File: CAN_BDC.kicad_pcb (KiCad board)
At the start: 2 copper layers, 25 x 31.8 mm, 28 parts, among them P1 CONN_01X02, P2 CONN_01X05, P3 CONN_01X02, P4 CONN_01X04, P5 CONN_01X04, P6 CONN_01X02, P7 CONN_01X04, P8 CONN_01X04, P9 CONN_01X02, U1 PSD2CAN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

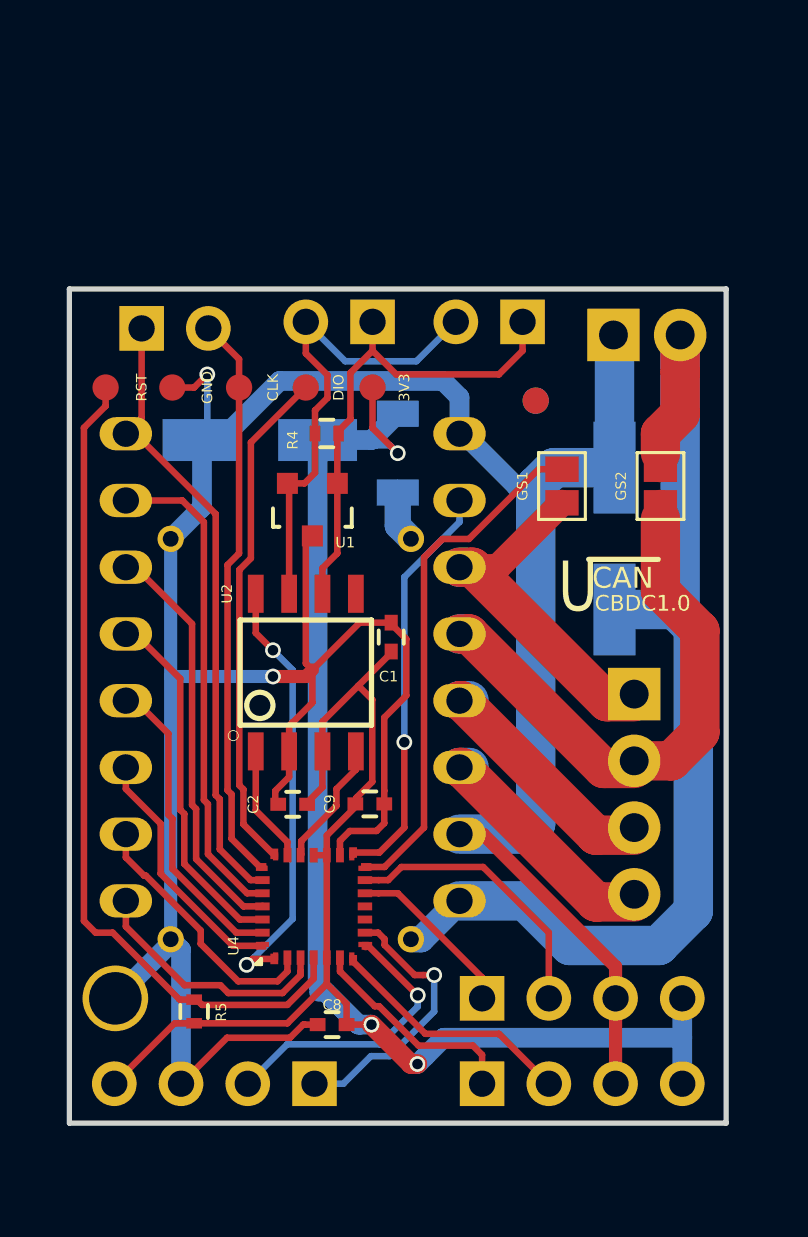
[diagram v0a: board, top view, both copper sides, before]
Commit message: Connector reposition
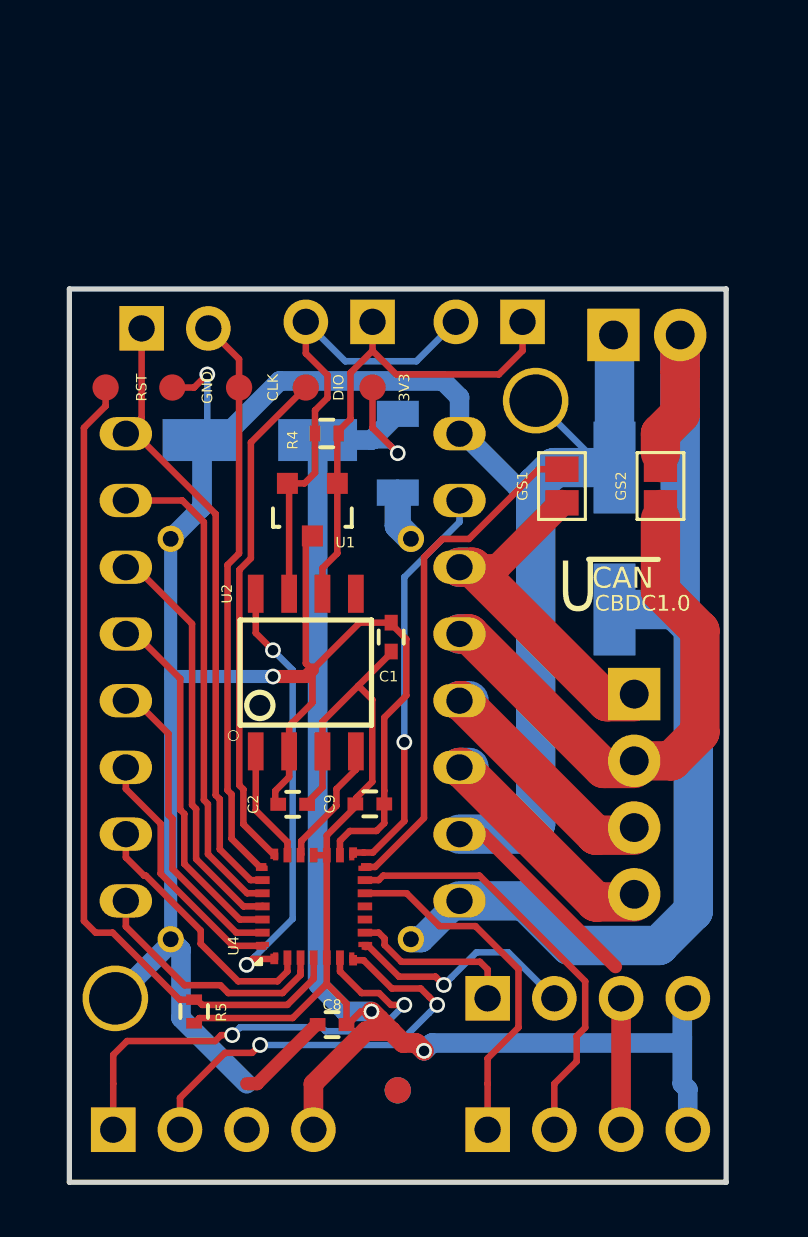
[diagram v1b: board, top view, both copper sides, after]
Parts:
- added mh2: fiducial, usb_ccb_custom:1pin, F.Cu at (156.4, 84.0)
- U3: value POLOLU_DRV8825 -> POLOLU_DRV8825/DRV8801
- moved f1 26.8 mm to (151.2, 110.3)
- moved f2 26.8 mm to (151.2, 110.3)
- moved P8 14.1 mm to (140.4, 111.8)
- moved P4 7.35 mm to (154.6, 106.8), turned to 270 degrees
- moved P5 5.00 mm to (154.6, 111.8)
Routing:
- net GPIO1: track 8.68 -> 18.3 mm, vias 0 -> 2
- net GPIO3: track 6.58 -> 13.6 mm
- net GPIO2: track 9.43 -> 16.4 mm, vias 0 -> 2
- net GPIO4: track 10.7 -> 16.3 mm
- net /USART_RX: track 10.5 -> 6.49 mm, vias 1 -> 0
- net GND: track 124.2 -> 126.7 mm
- net /USART_TX: track 10.9 -> 9.06 mm
- net +3V3: track 81.7 -> 82.7 mm
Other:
- board size 25 x 31.8 mm -> 25 x 34 mm

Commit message: CAN layout update
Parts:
- moved P3 1.50 mm to (141.4, 79.8)
- moved P1 1.25 mm to (150.2, 79.8)
- moved P9 1.25 mm to (155.9, 79.8)
- moved C7 0.15 mm to (146.1, 85.5)
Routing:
- net Net-(P1-Pad2): track 18.7 -> 22.2 mm
- net Net-(P1-Pad1): track 18.7 -> 20.9 mm
- net SW_CLK: track 21.7 -> 23.7 mm
- net DRV_DIR: track 24.7 -> 25.9 mm
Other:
- board size 25 x 34 mm -> 25 x 35.5 mm
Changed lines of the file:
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@@
   (general
     (links 85)
-    (no_connects 6)
-    (area 138.599999 79.699999 163.800001 113.900001)
+    (no_connects 2)
+    (area 138.599999 78.699999 163.800001 113.900001)
     (thickness 1.6)
     (drawings 13)
-    (tracks 391)
+    (tracks 403)
     (zones 0)
     (modules 29)
@@
   (page A4)
   (layers
-    (0 F.Cu signal hide)
-    (31 B.Cu signal hide)
+    (0 F.Cu signal)
+    (31 B.Cu signal)
     (32 B.Adhes user)
     (33 F.Adhes user)
@@
   )
   (module Capacitors_SMD:c_elec_5x5.8 (layer B.Cu)
-    (at 145.95 85.55 180)
+    (at 146.1 85.55 180)
     (descr "SMT capacitor, aluminium electrolytic, 5x5.8")
     (attr smd)
@@
   )
   (module Pin_Headers:Pin_Header_Straight_1x02_Pitch2.54mm (layer B.Cu)
-    (at 155.95 81.05 90)
+    (at 155.95 79.8 90)
     (descr "Through hole straight pin header, 1x02, 2.54mm pitch, single row")
     (tags "Through hole pin header THT 1x02 2.54mm single row")
@@
   )
   (module Pin_Headers:Pin_Header_Straight_1x02_Pitch2.54mm (layer B.Cu)
-    (at 150.24 81.05 90)
+    (at 150.24 79.8 90)
     (descr "Through hole straight pin header, 1x02, 2.54mm pitch, single row")
     (tags "Through hole pin header THT 1x02 2.54mm single row")
@@
   )
   (module Pin_Headers:Pin_Header_Straight_1x02_Pitch2.54mm (layer B.Cu)
-    (at 141.45 81.3 270)
+    (at 141.45 79.8 270)
     (descr "Through hole straight pin header, 1x02, 2.54mm pitch, single row")
     (tags "Through hole pin header THT 1x02 2.54mm single row")
@@
   )
   (gr_line (start 163.7 113.8) (end 138.7 113.8) (layer Edge.Cuts) (width 0.2))
-  (gr_line (start 163.7 79.8) (end 163.7 113.8) (layer Edge.Cuts) (width 0.2))
-  (gr_line (start 138.7 79.8) (end 163.7 79.8) (layer Edge.Cuts) (width 0.2))
-  (gr_line (start 138.7 113.8) (end 138.7 79.8) (layer Edge.Cuts) (width 0.2))
+  (gr_line (start 163.7 78.3) (end 163.7 113.8) (layer Edge.Cuts) (width 0.2))
+  (gr_line (start 138.7 78.3) (end 163.7 78.3) (layer Edge.Cuts) (width 0.2))
+  (gr_line (start 138.7 113.8) (end 138.7 78.3) (layer Edge.Cuts) (width 0.2))
   (gr_text GND (at 143.95 83.55 90) (layer F.SilkS)
     (effects (font (size 0.4 0.4) (thickness 0.1)))
@@
   )
   (gr_line (start 158.465484 90.090166) (end 161.111084 90.090166) (angle 90) (layer F.SilkS) (width 0.2))
+  (segment (start 147.7 81.05) (end 147.7 79.8) (width 0.25) (layer B.Cu) (net 1))
+  (segment (start 153.41 81.05) (end 153.41 79.8) (width 0.25) (layer B.Cu) (net 1))
+  (segment (start 147.7 82.252081) (end 147.7 81.3) (width 0.25) (layer F.Cu) (net 1))
+  (segment (start 147.7 81.3) (end 147.7 81.05) (width 0.25) (layer F.Cu) (net 1))
+  (segment (start 147.7 80.3) (end 147.7 81.3) (width 0.25) (layer F.Cu) (net 1))
   (segment (start 149.2 82.55) (end 151.91 82.55) (width 0.25) (layer B.Cu) (net 1))
   (segment (start 151.91 82.55) (end 153.41 81.05) (width 0.25) (layer B.Cu) (net 1))
@@
   (segment (start 148.525001 83.946001) (end 148.525001 83.077082) (width 0.25) (layer F.Cu) (net 1))
   (segment (start 148.525001 83.077082) (end 147.7 82.252081) (width 0.25) (layer F.Cu) (net 1))
-  (segment (start 147.7 82.252081) (end 147.7 81.05) (width 0.25) (layer F.Cu) (net 1))
   (segment (start 147 87.19924) (end 147.65005 87.19924) (width 0.25) (layer F.Cu) (net 1))
   (segment (start 147.65005 87.19924) (end 148.05 86.79929) (width 0.25) (layer F.Cu) (net 1))
@@
   (segment (start 148.5 101.35) (end 148 101.35) (width 0.25) (layer F.Cu) (net 3) (status 30))
   (segment (start 148.5 105.25) (end 148.5 101.593408) (width 0.25) (layer F.Cu) (net 3) (status 30))
+  (segment (start 143.99 80.8) (end 143.99 80.3) (width 0.25) (layer F.Cu) (net 4))
+  (segment (start 143.99 81.3) (end 143.99 80.8) (width 0.25) (layer F.Cu) (net 4))
+  (segment (start 143.99 80.8) (end 143.99 79.8) (width 0.25) (layer F.Cu) (net 4))
   (segment (start 145.16 83.55) (end 145.16 82.47) (width 0.25) (layer F.Cu) (net 4))
   (segment (start 145.16 82.47) (end 143.99 81.3) (width 0.25) (layer F.Cu) (net 4))
@@
   (segment (start 151.7 104.55) (end 152.09 104.55) (width 1) (layer B.Cu) (net 11) (status 30))
   (segment (start 152.09 104.55) (end 153.55 103.09) (width 1) (layer B.Cu) (net 11) (status 30))
+  (segment (start 155.95 81.05) (end 155.95 79.8) (width 0.25) (layer F.Cu) (net 12))
+  (segment (start 150.24 81.3) (end 150.24 81.05) (width 0.25) (layer F.Cu) (net 12))
+  (segment (start 150.24 81.3) (end 150.24 80.3) (width 0.25) (layer F.Cu) (net 12))
+  (segment (start 150.24 82.15) (end 150.24 81.3) (width 0.25) (layer F.Cu) (net 12))
   (segment (start 151.14 83.05) (end 155.05 83.05) (width 0.25) (layer F.Cu) (net 12))
   (segment (start 155.05 83.05) (end 155.95 82.15) (width 0.25) (layer F.Cu) (net 12))
@@
   (segment (start 149.4 84.75) (end 149.4 82.99) (width 0.25) (layer F.Cu) (net 12))
   (segment (start 148.95 85.2) (end 149.4 84.75) (width 0.25) (layer F.Cu) (net 12))
-  (segment (start 150.24 82.15) (end 150.24 81.05) (width 0.25) (layer F.Cu) (net 12))
   (segment (start 148.95 85.3) (end 148.95 85.2) (width 0.25) (layer F.Cu) (net 12))
   (segment (start 149.4 82.99) (end 150.24 82.15) (width 0.25) (layer F.Cu) (net 12))
@@
   (segment (start 143.975056 99.406753) (end 143.975056 101.310347) (width 0.25) (layer F.Cu) (net 15))
   (segment (start 145.464709 102.8) (end 146.05 102.8) (width 0.25) (layer F.Cu) (net 15) (status 20))
+  (segment (start 141.45 80.8) (end 141.45 80.3) (width 0.25) (layer F.Cu) (net 16))
+  (segment (start 141.45 81.3) (end 141.45 80.8) (width 0.25) (layer F.Cu) (net 16))
+  (segment (start 141.45 80.8) (end 141.45 79.8) (width 0.25) (layer F.Cu) (net 16))
   (segment (start 141.45 81.3) (end 141.45 84.71) (width 0.25) (layer F.Cu) (net 16))
   (segment (start 141.45 84.71) (end 140.85 85.31) (width 0.25) (layer F.Cu) (net 16))
@@
   (segment (start 144.269977 99.065263) (end 144.269977 88.364977) (width 0.25) (layer F.Cu) (net 16))
   (segment (start 144.269977 88.364977) (end 141.215 85.31) (width 0.25) (layer F.Cu) (net 16) (status 20))
-  (segment (start 140.85 81.9) (end 141.45 81.3) (width 0.25) (layer F.Cu) (net 16) (status 30))
   (segment (start 140.85 101.435) (end 141.54499 102.12999) (width 0.25) (layer F.Cu) (net 17))
   (segment (start 143.7 104.725002) (end 145.124976 106.149978) (width 0.25) (layer F.Cu) (net 17))
@@
     (polygon
       (pts
-        (xy 138.7 79.8) (xy 163.7 79.8) (xy 163.7 113.8) (xy 138.7 113.8)
+        (xy 138.7 78.3) (xy 163.7 78.3) (xy 163.7 113.8) (xy 138.7 113.8)
       )
     )
@@
     (polygon
       (pts
-        (xy 138.7 79.8) (xy 163.7 79.8) (xy 163.7 113.8) (xy 138.7 113.8)
+        (xy 138.7 78.3) (xy 163.7 78.3) (xy 163.7 113.8) (xy 138.7 113.8)
       )
     )

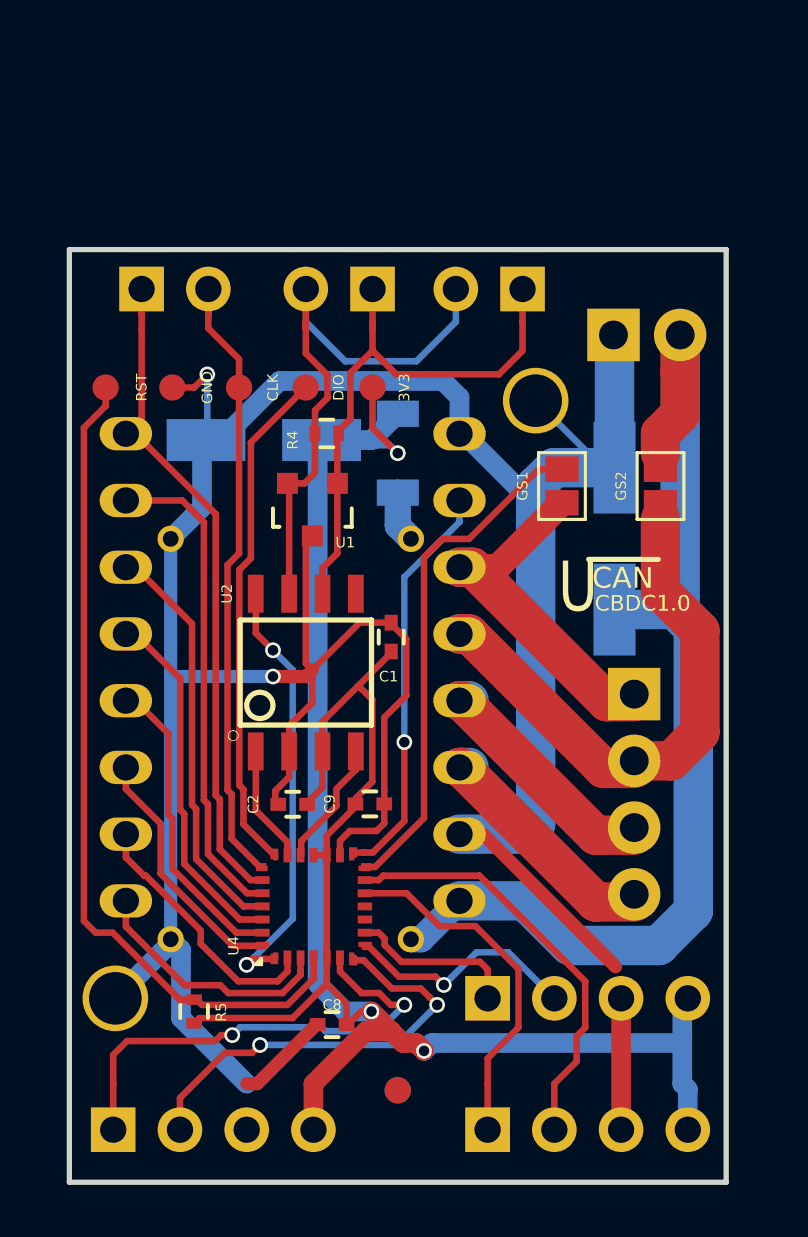
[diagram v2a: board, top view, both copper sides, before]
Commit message: Mini-360 Flip
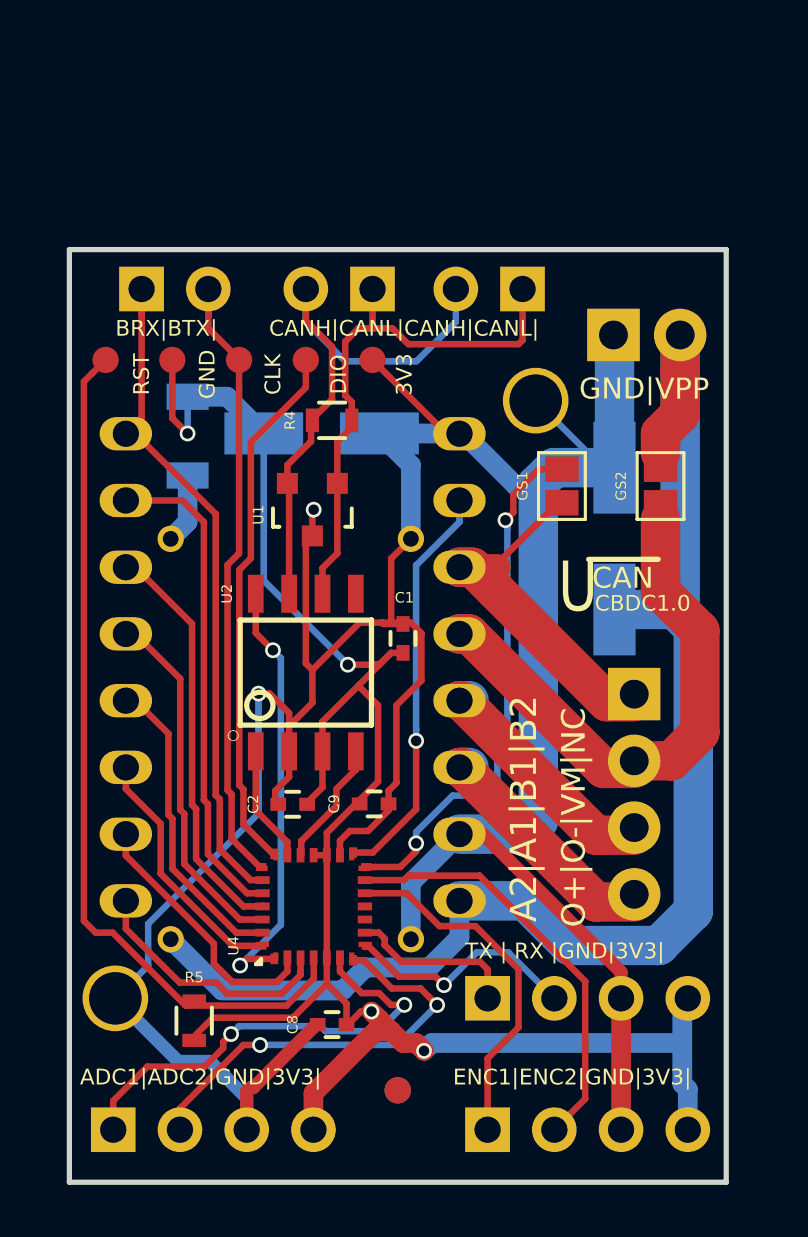
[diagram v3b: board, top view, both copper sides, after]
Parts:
- R4, R5: footprint Resistors_SMD:R_0402 -> Resistors_SMD:R_0603
- moved L2 8.03 mm to (143.2, 85.4)
- moved C7 2.21 mm to (148.3, 85.3), turned to 0 degrees
- moved P2 1.05 mm to (146.4, 82.5)
- moved R4 0.54 mm to (148.7, 84.8)
- moved C1 0.45 mm to (151.4, 93.1)
- moved R5 0.35 mm to (143.4, 107.7)
- moved C9 0.16 mm to (150.3, 99.4)
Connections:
- P2 pad 1: +3V3 -> GND
- P2 pad 4: GND -> +3V3
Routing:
- net VPP: track 43.4 -> 55.2 mm
- net +3V3: track 82.7 -> 72.7 mm, vias 3 -> 4
- net GND: track 126.7 -> 124.8 mm
- net Net-(P2-Pad5): track 31.9 -> 33.0 mm
- net SW_DIO: track 19.4 -> 20.5 mm
- net DRV8801_CS: track 14.1 -> 15.1 mm
- net GPIO1: track 18.3 -> 17.5 mm
- net Net-(L2-Pad1): track 1.97 -> 2.68 mm
- net Net-(GS1-Pad1): track 19.5 -> 20.2 mm, vias 0 -> 2
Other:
- board text added: "A2|A1|B1|B2"
- board text added: "ADC1|ADC2|GND|3V3|"
- board text added: "BRX|BTX|"
- board text added: "CANH|CANL|CANH|CANL|"
- board text added: "ENC1|ENC2|GND|3V3|"
- board text added: "GND|VPP"
- board text added: "O+|O-|VM|NC"
- board text added: "TX | RX |GND|3V3|"

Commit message: ZL321 Footprint add
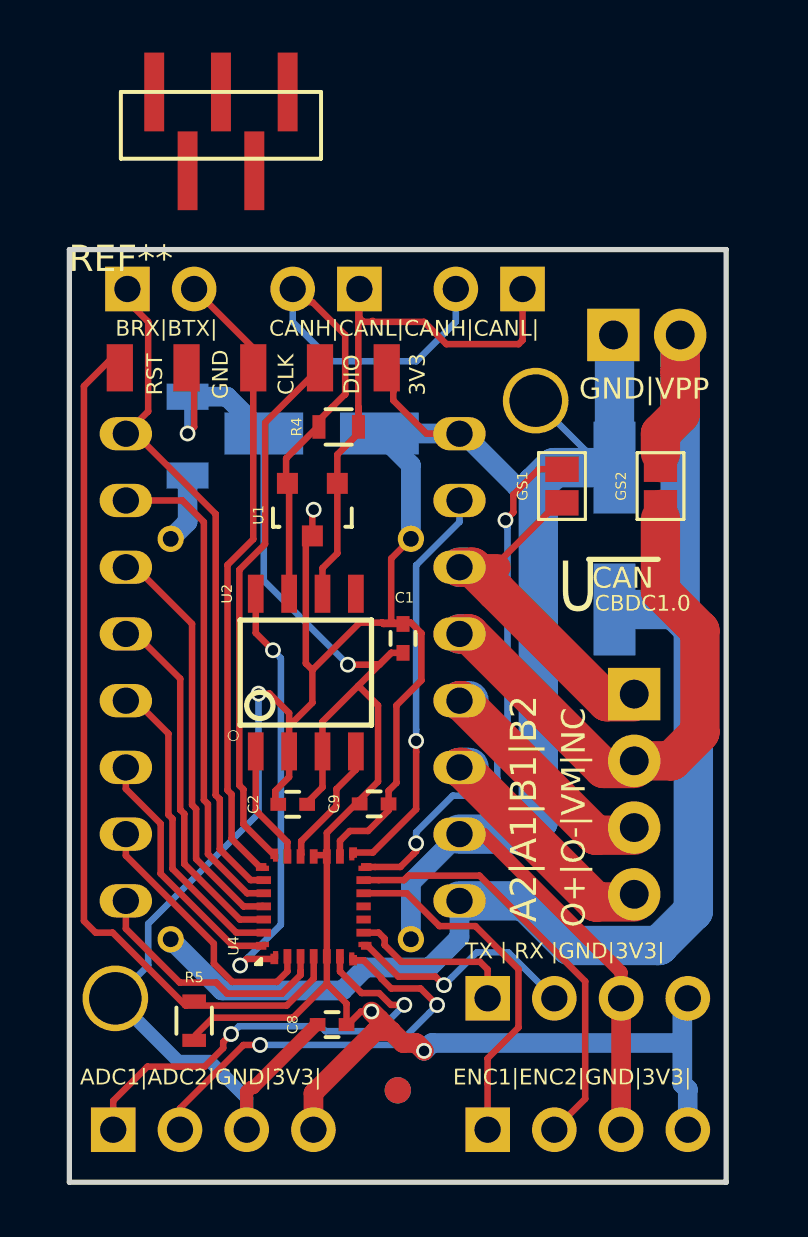
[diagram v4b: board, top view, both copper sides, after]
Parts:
- added REF**: ZL321-5P, usb_ccb_custom:ZL321-5P, F.Cu at (141.9, 72.3)
- moved P2 0.62 mm to (147.0, 82.8)
- moved P3 0.54 mm to (140.9, 79.8)
- moved P1 0.50 mm to (149.7, 79.8)
- moved R4 0.35 mm to (148.9, 85.0)
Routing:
- net Net-(P1-Pad1): track 20.7 -> 22.5 mm
- net Net-(P1-Pad2): track 21.8 -> 23.1 mm
- net SW_CLK: track 23.7 -> 24.5 mm
- net Net-(P2-Pad5): track 33.0 -> 33.7 mm
- net GND: track 124.8 -> 125.4 mm

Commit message: Size reduction
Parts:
- removed P3: CONN_01X02, Pin_Headers:Pin_Header_Straight_1x02_Pitch2.54mm
- removed REF**: ZL321-5P, usb_ccb_custom:ZL321-5P
- R5: footprint Resistors_SMD:R_0603 -> Resistors_SMD:R_0402
- moved P1 2.50 mm to (147.2, 79.8)
- moved P9 1.96 mm to (154.0, 79.8)
- moved P6 1.48 mm to (157.9, 81.3)
- moved P5 1.10 mm to (154.2, 110.8)
- moved P8 1.00 mm to (140.4, 110.8)
- moved P4 0.42 mm to (154.2, 106.8)
- moved R5 0.35 mm to (143.4, 107.3)
- moved C8 0.25 mm to (148.7, 107.5)
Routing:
- net DRV_DIR: track 25.8 -> 19.6 mm
- net SW_CLK: track 24.5 -> 21.3 mm
- net Net-(P1-Pad1): track 22.5 -> 19.8 mm
- net GND: track 125.4 -> 123.3 mm
- net GPIO2: track 16.1 -> 14.5 mm
- net +3V3: track 72.5 -> 71.0 mm
- net DRV8801_CS: track 15.1 -> 13.6 mm
- net Net-(P1-Pad2): track 23.1 -> 24.4 mm
- net GPIO1: track 17.5 -> 16.2 mm
- net GPIO4: track 16.3 -> 15.2 mm
- net /USART_RX: track 6.49 -> 5.85 mm
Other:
- board size 25 x 35.5 mm -> 24.5 x 34 mm
- board text added: "CANH|CANL | CANH|CANL|"
- board text removed: "BRX|BTX|"
- board text removed: "CANH|CANL|CANH|CANL|"
